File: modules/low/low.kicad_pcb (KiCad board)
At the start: 2 copper layers, 30.5 x 68.6 mm, 23 parts, among them SW1 SPST_TS-1187A-B-A-B, U1 VTL5C, U2 MCP6002-xSN, U3 VTL5C, U5 MCP6002-xSN

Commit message: low_1.0.0
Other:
- board text added: "LOW 1.0.0"
- board text removed: "LOW 0.1.0"
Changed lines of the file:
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@@
 		)
 	)
-	(gr_text "LOW\n0.1.0"
+	(gr_text "LOW\n1.0.0"
 		(at 76.327 107.95 0)
 		(layer "F.SilkS")

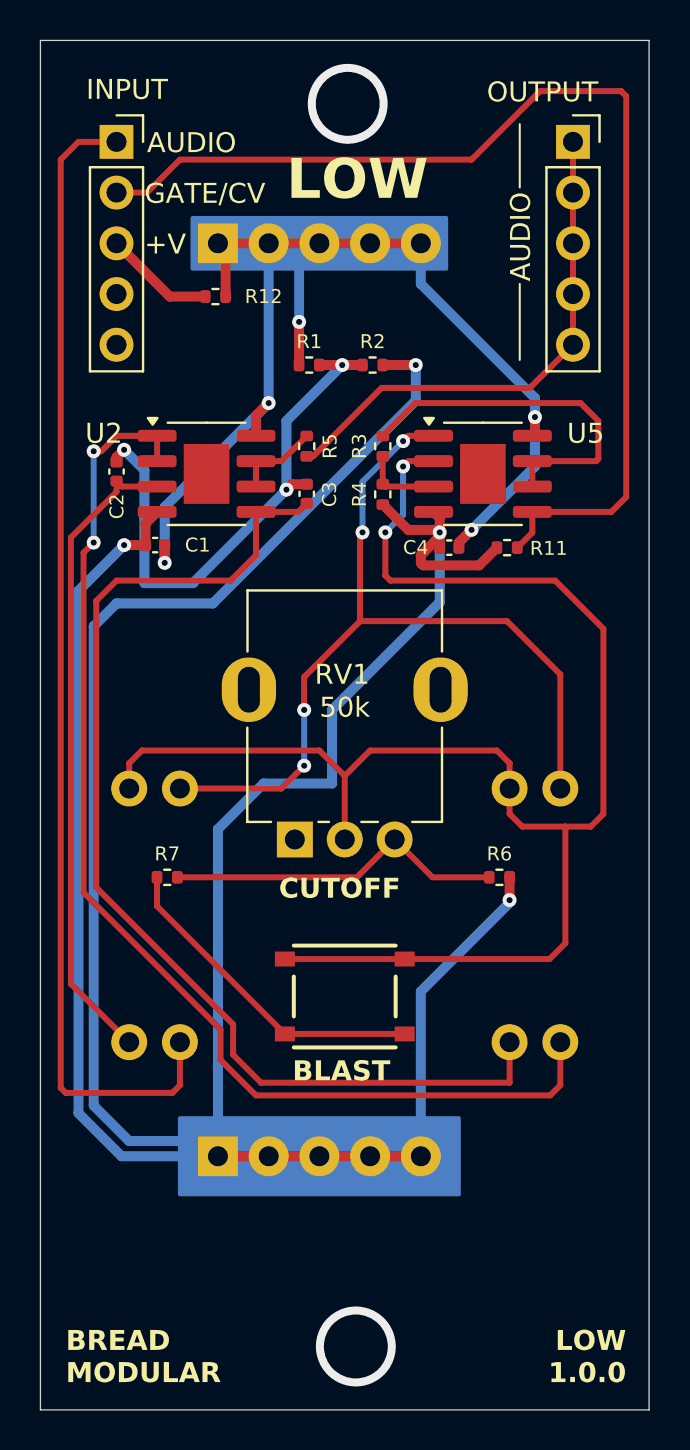
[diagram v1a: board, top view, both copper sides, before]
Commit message: low: Change the push button
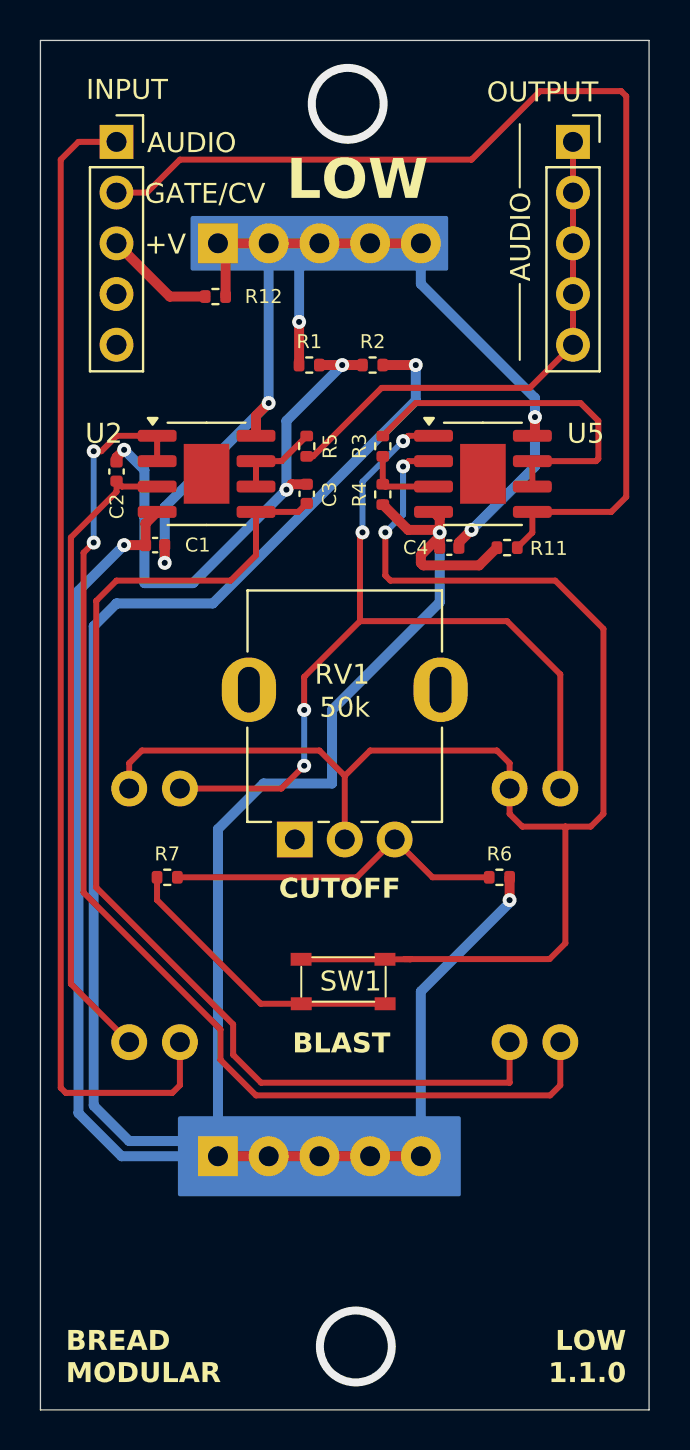
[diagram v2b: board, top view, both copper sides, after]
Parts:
- SW1: value SPST_TS-1187A-B-A-B -> K2-1808SN-A4SW-01; footprint BreadModular_MISC:SPST_TS-1187A-B-A-B -> BreadModular_MISC:K2-1808SN-A4SW-01
- moved SW1 0.77 mm to (62.1, 87.8)
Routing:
- net Net-(SW1-B): track 16.5 -> 14.7 mm
- net VAC_NEG: track 81.8 -> 81.3 mm
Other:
- board text added: "LOW 1.1.0"
- board text removed: "LOW 1.0.0"
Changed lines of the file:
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@@
 		(property ki_fp_filters "SOIC*3.9x4.9mm*P1.27mm* DIP*W7.62mm* TO*99* OnSemi*Micro8* TSSOP*3x3mm*P0.65mm* TSSOP*4.4x3mm*P0.65mm* MSOP*3x3mm*P0.65mm* SSOP*3.9x4.9mm*P0.635mm* LFCSP*2x2mm*P0.5mm* *SIP* SOIC*5.3x6.2mm*P1.27mm*")
 		(sheetname "Root")
-		(sheetfile "low_pass.kicad_sch")
+		(sheetfile "low.kicad_sch")
 		(attr smd)
 		(fp_line
@@
 		(property ki_fp_filters "R_*")
 		(sheetname "Root")
-		(sheetfile "low_pass.kicad_sch")
+		(sheetfile "low.kicad_sch")
 		(attr smd)
 		(fp_line
@@
 		(property ki_fp_filters "R_*")
 		(sheetname "Root")
-		(sheetfile "low_pass.kicad_sch")
+		(sheetfile "low.kicad_sch")
 		(attr smd)
 		(fp_line
@@
 		(property ki_fp_filters "R_*")
 		(sheetname "Root")
-		(sheetfile "low_pass.kicad_sch")
+		(sheetfile "low.kicad_sch")
 		(attr smd)
 		(fp_line
@@
 		(property ki_fp_filters "R_*")
 		(sheetname "Root")
-		(sheetfile "low_pass.kicad_sch")
+		(sheetfile "low.kicad_sch")
 		(attr smd)
 		(fp_line
@@
 		(property ki_fp_filters "Potentiometer*")
 		(sheetname "Root")
-		(sheetfile "low_pass.kicad_sch")
+		(sheetfile "low.kicad_sch")
 		(attr through_hole)
 		(fp_line
@@
 		(property ki_fp_filters "C_*")
 		(sheetname "Root")
-		(sheetfile "low_pass.kicad_sch")
+		(sheetfile "low.kicad_sch")
 		(attr smd)
 		(fp_line
@@
 		(property ki_fp_filters "Connector*:*_1x??_*")
 		(sheetname "Root")
-		(sheetfile "low_pass.kicad_sch")
+		(sheetfile "low.kicad_sch")
 		(attr through_hole)
 		(fp_line
@@
 		(property ki_fp_filters "SOIC*3.9x4.9mm*P1.27mm* DIP*W7.62mm* TO*99* OnSemi*Micro8* TSSOP*3x3mm*P0.65mm* TSSOP*4.4x3mm*P0.65mm* MSOP*3x3mm*P0.65mm* SSOP*3.9x4.9mm*P0.635mm* LFCSP*2x2mm*P0.5mm* *SIP* SOIC*5.3x6.2mm*P1.27mm*")
 		(sheetname "Root")
-		(sheetfile "low_pass.kicad_sch")
+		(sheetfile "low.kicad_sch")
 		(attr smd)
 		(fp_line
@@
 		(property ki_fp_filters "R_*")
 		(sheetname "Root")
-		(sheetfile "low_pass.kicad_sch")
+		(sheetfile "low.kicad_sch")
 		(attr smd)
 		(fp_line
@@
 		(property ki_fp_filters "R_*")
 		(sheetname "Root")
-		(sheetfile "low_pass.kicad_sch")
+		(sheetfile "low.kicad_sch")
 		(attr smd)
 		(fp_line
@@
 		)
 	)
-	(footprint "BreadModular_MISC:SPST_TS-1187A-B-A-B"
+	(footprint "BreadModular_MISC:K2-1808SN-A4SW-01"
 		(layer "F.Cu")
-		(at 62.23 88.519)
+		(at 62.103 87.757)
 		(property "Reference" "SW1"
-			(at 0.032 3.163 0)
-			(layer "F.Fab")
+			(at 0.425 0 0)
+			(unlocked yes)
+			(layer "F.SilkS")
 			(effects
 				(font
-					(size 0.5 0.5)
-					(thickness 0.12)
+					(size 1 1)
+					(thickness 0.1)
 				)
 			)
 		)
-		(property "Value" "SPST_TS-1187A-B-A-B"
-			(at 0 0 0)
+		(property "Value" "K2-1808SN-A4SW-01"
+			(at 0.025 2.6 0)
+			(unlocked yes)
 			(layer "F.Fab")
 			(effects
 				(font
-					(size 0.5 0.5)
-					(thickness 0.12)
+					(size 1 1)
+					(thickness 0.15)
 				)
 			)
 		)
-		(property "Footprint" "BreadModular_MISC:SPST_TS-1187A-B-A-B"
-			(at 0 0 0)
+		(property "Footprint" "BreadModular_MISC:K2-1808SN-A4SW-01"
+			(at 2.26 1.125 0)
+			(unlocked yes)
 			(layer "F.Fab")
 			(hide yes)
 			(effects
 				(font
-					(size 1.27 1.27)
+					(size 1 1)
 					(thickness 0.15)
 				)
@@
 		)
 		(property "Datasheet" ""
-			(at 0 0 0)
+			(at 2.26 1.125 0)
+			(unlocked yes)
 			(layer "F.Fab")
 			(hide yes)
 			(effects
 				(font
-					(size 1.27 1.27)
+					(size 1 1)
 					(thickness 0.15)
 				)
@@
 		)
 		(property "Description" "Single Pole Single Throw (SPST) switch"
-			(at 0 0 0)
+			(at 2.26 1.125 0)
+			(unlocked yes)
 			(layer "F.Fab")
 			(hide yes)
 			(effects
 				(font
-					(size 1.27 1.27)
+					(size 1 1)
 					(thickness 0.15)
 				)
@@
 		)
 		(sheetname "Root")
-		(sheetfile "low_pass.kicad_sch")
-		(attr through_hole)
+		(sheetfile "low.kicad_sch")
+		(attr smd)
 		(fp_line
-			(start -2.55 -2.55)
-			(end 2.55 -2.55)
+			(start -2.05 -0.725)
+			(end -2.05 0.775)
 			(stroke
-				(width 0.2)
-				(type solid)
+				(width 0.1)
+				(type default)
 			)
 			(layer "F.SilkS")
 		)
 		(fp_line
-			(start -2.55 -1)
-			(end -2.55 1)
+			(start -1.5 -1.2)
+			(end 1.6 -1.2)
 			(stroke
-				(width 0.2)
-				(type solid)
+				(width 0.1)
+				(type default)
 			)
 			(layer "F.SilkS")
 		)
 		(fp_line
-			(start -2.55 2.55)
-			(end 2.55 2.55)
+			(start -1.49 1.025)
+			(end 1.61 1.025)
 			(stroke
-				(width 0.2)
-				(type solid)
+				(width 0.1)
+				(type default)
 			)
 			(layer "F.SilkS")
 		)
 		(fp_line
-			(start 2.55 -1)
-			(end 2.55 1)
+			(start 2.175 -0.725)
+			(end 2.175 0.775)
 			(stroke
-				(width 0.2)
-				(type solid)
+				(width 0.1)
+				(type default)
 			)
 			(layer "F.SilkS")
 		)
+		(fp_text user "${REFERENCE}"
+			(at 0.025 4.1 0)
+			(unlocked yes)
+			(layer "F.Fab")
+			(effects
+				(font
+					(size 1 1)
+					(thickness 0.15)
+				)
+			)
+		)
 		(pad "1" smd rect
-			(at -3 -1.875)
-			(size 1 0.75)
+			(at -2.06 -1.1)
+			(size 1.05 0.65)
 			(layers "F.Cu" "F.Paste" "F.Mask")
 			(net 16 "VAC_NEG")
 			(pinfunction "A")
 			(pintype "passive")
+			(thermal_bridge_angle 45)
 		)
 		(pad "1" smd rect
-			(at 3 -1.875)
-			(size 1 0.75)
+			(at 2.14 -1.1)
+			(size 1.05 0.65)
 			(layers "F.Cu" "F.Paste" "F.Mask")
 			(net 16 "VAC_NEG")
 			(pinfunction "A")
 			(pintype "passive")
+			(thermal_bridge_angle 45)
 		)
 		(pad "2" smd rect
-			(at -3 1.875)
-			(size 1 0.75)
+			(at -2.05 1.125)
+			(size 1.05 0.65)
 			(layers "F.Cu" "F.Paste" "F.Mask")
 			(net 12 "Net-(SW1-B)")
 			(pinfunction "B")
 			(pintype "passive")
+			(thermal_bridge_angle 45)
 		)
 		(pad "2" smd rect
-			(at 3 1.875)
-			(size 1 0.75)
+			(at 2.15 1.125)
+			(size 1.05 0.65)
 			(layers "F.Cu" "F.Paste" "F.Mask")
 			(net 12 "Net-(SW1-B)")
 			(pinfunction "B")
 			(pintype "passive")
+			(thermal_bridge_angle 45)
 		)
 	)
@@
 		(property ki_fp_filters "C_*")
 		(sheetname "Root")
-		(sheetfile "low_pass.kicad_sch")
+		(sheetfile "low.kicad_sch")
 		(attr smd)
 		(fp_line
@@
 		(property ki_fp_filters "C_*")
 		(sheetname "Root")
-		(sheetfile "low_pass.kicad_sch")
+		(sheetfile "low.kicad_sch")
 		(attr smd)
 		(fp_line
@@
 		(property ki_fp_filters "R_*")
 		(sheetname "Root")
-		(sheetfile "low_pass.kicad_sch")
+		(sheetfile "low.kicad_sch")
 		(attr smd)
 		(fp_line
@@
 		(property ki_fp_filters "R_*")
 		(sheetname "Root")
-		(sheetfile "low_pass.kicad_sch")
+		(sheetfile "low.kicad_sch")
 		(attr smd)
 		(fp_line
@@
 		(property ki_fp_filters "R_*")
 		(sheetname "Root")
-		(sheetfile "low_pass.kicad_sch")
+		(sheetfile "low.kicad_sch")
 		(attr smd)
 		(fp_line
@@
 		(property ki_fp_filters "C_*")
 		(sheetname "Root")
-		(sheetfile "low_pass.kicad_sch")
+		(sheetfile "low.kicad_sch")
 		(attr smd)
 		(fp_line
@@
 		(property ki_fp_filters "Connector*:*_1x??_*")
 		(sheetname "Root")
-		(sheetfile "low_pass.kicad_sch")
+		(sheetfile "low.kicad_sch")
 		(attr through_hole)
 		(fp_line
@@
 		(property ki_fp_filters "PerkinElmer*VTL5C*")
 		(sheetname "Root")
-		(sheetfile "low_pass.kicad_sch")
+		(sheetfile "low.kicad_sch")
 		(attr through_hole)
 		(fp_line
@@
 		(property ki_fp_filters "PerkinElmer*VTL5C*")
 		(sheetname "Root")
-		(sheetfile "low_pass.kicad_sch")
+		(sheetfile "low.kicad_sch")
 		(attr through_hole)
 		(fp_line
@@
 		(property ki_fp_filters "Connector*:*_1x??_*")
 		(sheetname "Root")
-		(sheetfile "low_pass.kicad_sch")
+		(sheetfile "low.kicad_sch")
 		(attr through_hole)
 		(fp_line
@@
 		(property ki_fp_filters "Connector*:*_1x??_*")
 		(sheetname "Root")
-		(sheetfile "low_pass.kicad_sch")
+		(sheetfile "low.kicad_sch")
 		(attr through_hole)
 		(fp_line
@@
 	)
 	(gr_text "BLAST"
-		(at 64.516 92.837 0)
+		(at 64.516 91.44 0)
 		(layer "F.SilkS")
 		(effects
@@
 		)
 	)
-	(gr_text "LOW\n1.0.0"
+	(gr_text "LOW\n1.1.0"
 		(at 76.327 107.95 0)
 		(layer "F.SilkS")
@@
 	)
 	(segment
-		(start 65.23 90.394)
-		(end 59.23 90.394)
+		(start 58.021 88.882)
+		(end 52.83 83.691)
 		(width 0.3)
 		(layer "F.Cu")
@@
 	)
 	(segment
-		(start 52.83 82.55)
-		(end 52.83 83.994)
+		(start 52.83 83.691)
+		(end 52.83 82.55)
 		(width 0.3)
 		(layer "F.Cu")
@@
 	)
 	(segment
-		(start 52.83 83.994)
-		(end 59.23 90.394)
+		(start 60.053 88.882)
+		(end 58.021 88.882)
+		(width 0.3)
+		(layer "F.Cu")
+		(net 12)
+	)
+	(segment
+		(start 60.053 88.882)
+		(end 64.253 88.882)
 		(width 0.3)
 		(layer "F.Cu")
@@
 	)
 	(segment
+		(start 65.519 86.657)
+		(end 65.532 86.644)
+		(width 0.3)
+		(layer "F.Cu")
+		(net 16)
+	)
+	(segment
 		(start 73.279 80.01)
 		(end 71.12 80.01)
@@
 	)
 	(segment
+		(start 60.043 86.657)
+		(end 65.519 86.657)
+		(width 0.3)
+		(layer "F.Cu")
+		(net 16)
+	)
+	(segment
 		(start 70.485 76.835)
 		(end 70.485 78.105)
@@
 	)
 	(segment
+		(start 65.23 86.644)
+		(end 65.532 86.644)
+		(width 0.3)
+		(layer "F.Cu")
+		(net 16)
+	)
+	(segment
 		(start 51.435 78.105)
 		(end 51.435 76.835)
@@
 	)
 	(segment
-		(start 59.23 86.644)
-		(end 65.23 86.644)
-		(width 0.3)
-		(layer "F.Cu")
-		(net 16)
-	)
-	(segment
-		(start 65.23 86.644)
+		(start 65.532 86.644)
 		(end 72.487 86.644)
 		(width 0.3)
